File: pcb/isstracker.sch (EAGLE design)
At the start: 26 parts, among them IC2 L7805CV, J1 MOTOR_RIGHT, J2 MOTOR, J3 MOTOR_LEFT, J4 DISPLAY, J5 GLOBE_RESET, J6 CONTROL, J8 UART, J9 DISTANCE, Q2 60V/32A/35mΩ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

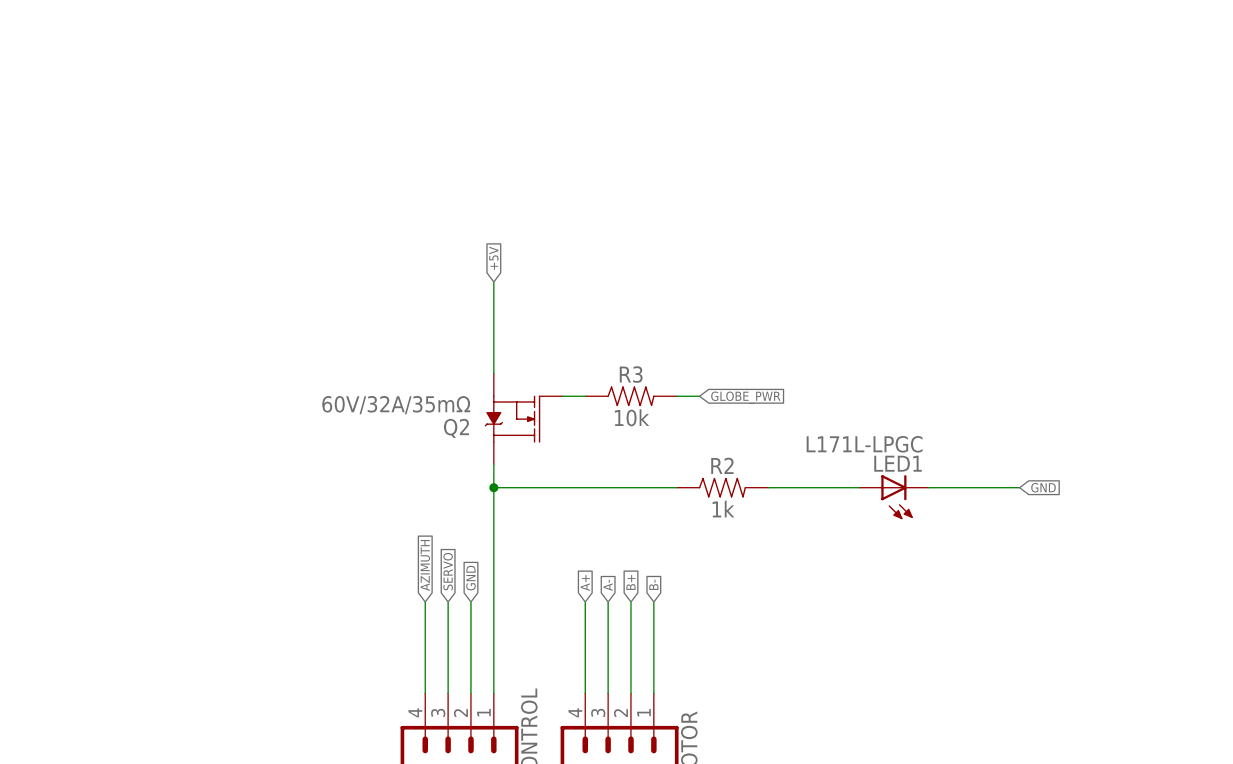
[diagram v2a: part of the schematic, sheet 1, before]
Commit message: Update to version 1.9
* Fix the FET, it wasn't right
* New FET in the BOM
* Put FET on low side and add pulldown on gate
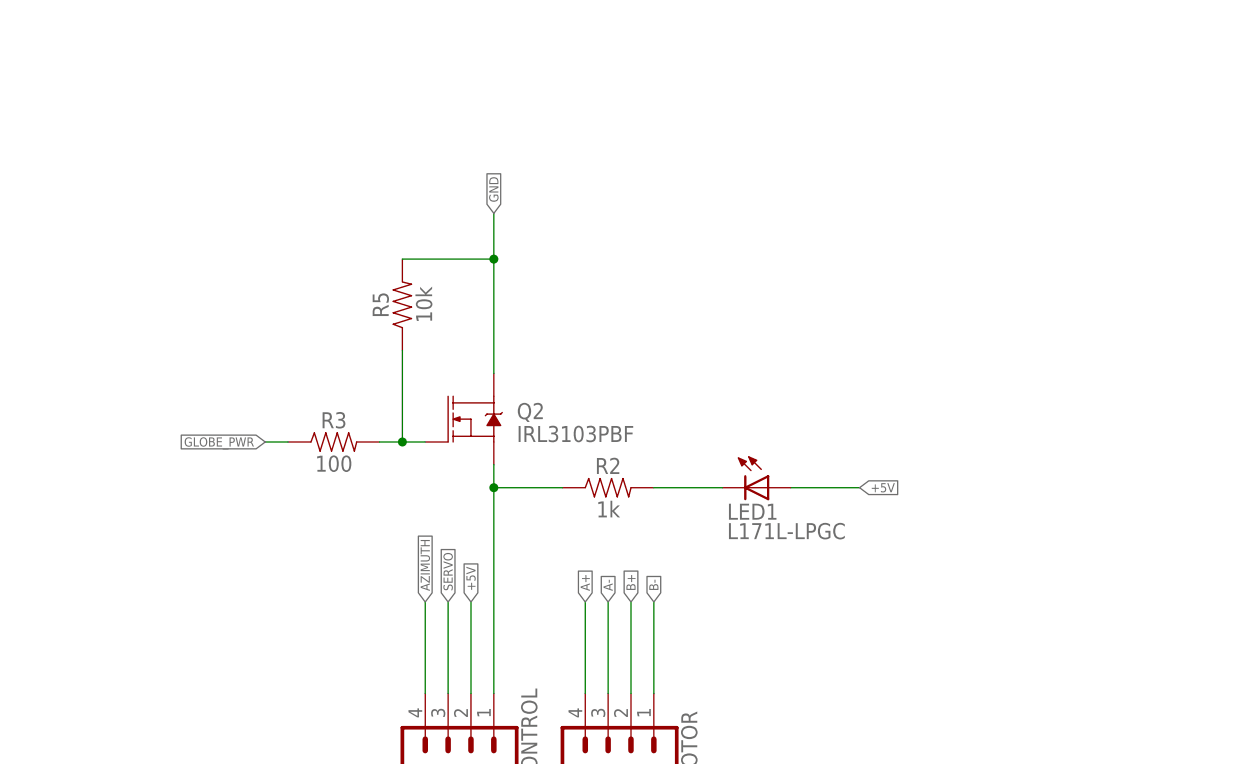
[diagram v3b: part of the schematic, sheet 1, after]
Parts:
- added R5: 10k, SparkFun-Resistors:0.75OHM-0805-1/4W-1%
- Q2: value 60V/32A/35mΩ -> IRL3103PBF
- R3: value 10k -> 100
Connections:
- removed net N$3: J6.1, Q2.D, R2.1
- removed net N$6: Q2.G, R3.1
- new net N$5: Q2.G, R3.2, R5.1
- new net N$8: J6.1, Q2.S, R2.1
- net +5V: now also J6.2, LED1.A; no longer Q2.S
- net GLOBE_PWR: now also R3.1; no longer R3.2
- net GND: now also Q2.D, R5.2; no longer J6.2, LED1.C
- net N$4: now also LED1.C; no longer LED1.A
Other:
- moved on the sheet: LED1, Q2, R2, R3
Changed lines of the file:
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@@
 <part name="J2" library="SparkFun-Connectors" library_urn="urn:adsk.eagle:library:513" deviceset="CONN_04" device="" package3d_urn="urn:adsk.eagle:package:38085/1" value="MOTOR"/>
 <part name="J6" library="SparkFun-Connectors" library_urn="urn:adsk.eagle:library:513" deviceset="CONN_04" device="" package3d_urn="urn:adsk.eagle:package:38085/1" value="CONTROL"/>
-<part name="Q2" library="SparkFun-DiscreteSemi" library_urn="urn:adsk.eagle:library:514" deviceset="MOSFET-NCH" device="-FQP30N06L" package3d_urn="urn:adsk.eagle:package:38447/1" value="60V/32A/35mΩ"/>
+<part name="Q2" library="SparkFun-DiscreteSemi" library_urn="urn:adsk.eagle:library:514" deviceset="MOSFET-NCH" device="-FQP30N06L" package3d_urn="urn:adsk.eagle:package:38447/1" value="IRL3103PBF "/>
 <part name="R2" library="SparkFun-Resistors" library_urn="urn:adsk.eagle:library:532" deviceset="0.75OHM" device="-0805-1/4W-1%" package3d_urn="urn:adsk.eagle:package:39651/1" value="1k"/>
 <part name="H6" library="holes" library_urn="urn:adsk.eagle:library:237" deviceset="MOUNT-HOLE" device="2.8" package3d_urn="urn:adsk.eagle:package:14271/1"/>
-<part name="R3" library="SparkFun-Resistors" library_urn="urn:adsk.eagle:library:532" deviceset="0.75OHM" device="-0805-1/4W-1%" package3d_urn="urn:adsk.eagle:package:39651/1" value="10k"/>
 <part name="LED3" library="adafruit" library_urn="urn:adsk.eagle:library:420" deviceset="LED" device="CHIPLED_1206" package3d_urn="urn:adsk.eagle:package:6240560/1" value="L171L-LPGC"/>
 <part name="LED1" library="adafruit" library_urn="urn:adsk.eagle:library:420" deviceset="LED" device="CHIPLED_1206" package3d_urn="urn:adsk.eagle:package:6240560/1" value="L171L-LPGC"/>
 <part name="J5" library="SparkFun-Connectors" library_urn="urn:adsk.eagle:library:513" deviceset="CONN_02" device="" package3d_urn="urn:adsk.eagle:package:38039/1" value="GLOBE_RESET"/>
 <part name="R4" library="SparkFun-Resistors" library_urn="urn:adsk.eagle:library:532" deviceset="0.75OHM" device="-0805-1/4W-1%" package3d_urn="urn:adsk.eagle:package:39651/1" value="10k"/>
+<part name="R5" library="SparkFun-Resistors" library_urn="urn:adsk.eagle:library:532" deviceset="0.75OHM" device="-0805-1/4W-1%" package3d_urn="urn:adsk.eagle:package:39651/1" value="10k"/>
+<part name="R3" library="SparkFun-Resistors" library_urn="urn:adsk.eagle:library:532" deviceset="0.75OHM" device="-0805-1/4W-1%" package3d_urn="urn:adsk.eagle:package:39651/1" value="100"/>
 </parts>
 <sheets>
@@
 <attribute name="NAME" x="101.092" y="33.02" size="1.778" layer="95" font="vector" rot="R90"/>
 </instance>
-<instance part="Q2" gate="NMOS" x="114.3" y="73.66" smashed="yes" rot="R180">
-<attribute name="NAME" x="109.22" y="73.66" size="1.778" layer="95" font="vector" rot="R180"/>
-<attribute name="VALUE" x="109.22" y="76.2" size="1.778" layer="96" font="vector" rot="R180"/>
-</instance>
-<instance part="R2" gate="G$1" x="137.16" y="66.04" smashed="yes">
-<attribute name="NAME" x="137.16" y="67.564" size="1.778" layer="95" font="vector" align="bottom-center"/>
-<attribute name="VALUE" x="137.16" y="64.516" size="1.778" layer="96" font="vector" align="top-center"/>
-</instance>
-<instance part="R3" gate="G$1" x="127" y="76.2" smashed="yes">
-<attribute name="NAME" x="127" y="77.724" size="1.778" layer="95" font="vector" align="bottom-center"/>
-<attribute name="VALUE" x="127" y="74.676" size="1.778" layer="96" font="vector" align="top-center"/>
-</instance>
-<instance part="LED1" gate="G$1" x="154.94" y="66.04" smashed="yes" rot="R90">
-<attribute name="NAME" x="159.512" y="69.596" size="1.778" layer="95" rot="R180"/>
-<attribute name="VALUE" x="159.512" y="71.755" size="1.778" layer="96" rot="R180"/>
+<instance part="Q2" gate="NMOS" x="109.22" y="73.66" smashed="yes">
+<attribute name="NAME" x="114.3" y="73.66" size="1.778" layer="95" font="vector"/>
+<attribute name="VALUE" x="114.3" y="71.12" size="1.778" layer="96" font="vector"/>
+</instance>
+<instance part="R2" gate="G$1" x="124.46" y="66.04" smashed="yes">
+<attribute name="NAME" x="124.46" y="67.564" size="1.778" layer="95" font="vector" align="bottom-center"/>
+<attribute name="VALUE" x="124.46" y="64.516" size="1.778" layer="96" font="vector" align="top-center"/>
+</instance>
+<instance part="LED1" gate="G$1" x="142.24" y="66.04" smashed="yes" rot="R270">
+<attribute name="NAME" x="137.668" y="62.484" size="1.778" layer="95"/>
+<attribute name="VALUE" x="137.668" y="60.325" size="1.778" layer="96"/>
 </instance>
 <instance part="J5" gate="G$1" x="12.7" y="116.84" smashed="yes">
@@
 <attribute name="NAME" x="28.956" y="111.76" size="1.778" layer="95" font="vector" rot="R90" align="bottom-center"/>
 <attribute name="VALUE" x="32.004" y="111.76" size="1.778" layer="96" font="vector" rot="R90" align="top-center"/>
+</instance>
+<instance part="R5" gate="G$1" x="101.6" y="86.36" smashed="yes" rot="R90">
+<attribute name="NAME" x="100.076" y="86.36" size="1.778" layer="95" font="vector" rot="R90" align="bottom-center"/>
+<attribute name="VALUE" x="103.124" y="86.36" size="1.778" layer="96" font="vector" rot="R90" align="top-center"/>
+</instance>
+<instance part="R3" gate="G$1" x="93.98" y="71.12" smashed="yes">
+<attribute name="NAME" x="93.98" y="72.644" size="1.778" layer="95" font="vector" align="bottom-center"/>
+<attribute name="VALUE" x="93.98" y="69.596" size="1.778" layer="96" font="vector" align="top-center"/>
 </instance>
 </instances>
@@
 </segment>
 <segment>
-<wire x1="109.22" y1="43.18" x2="109.22" y2="53.34" width="0.1524" layer="91"/>
-<label x="109.22" y="53.34" size="1.016" layer="95" rot="R90" xref="yes"/>
-<pinref part="J6" gate="G$1" pin="2"/>
-</segment>
-<segment>
-<wire x1="160.02" y1="66.04" x2="170.18" y2="66.04" width="0.1524" layer="91"/>
-<label x="170.18" y="66.04" size="1.016" layer="95" xref="yes"/>
-<pinref part="LED1" gate="G$1" pin="C"/>
-</segment>
-<segment>
 <pinref part="J3" gate="G$1" pin="12"/>
 <wire x1="20.32" y1="160.02" x2="27.94" y2="160.02" width="0.1524" layer="91"/>
@@
 <label x="43.18" y="119.38" size="1.016" layer="95" xref="yes"/>
 </segment>
+<segment>
+<pinref part="Q2" gate="NMOS" pin="D"/>
+<pinref part="R5" gate="G$1" pin="2"/>
+<wire x1="111.76" y1="78.74" x2="111.76" y2="91.44" width="0.1524" layer="91"/>
+<wire x1="111.76" y1="91.44" x2="111.76" y2="96.52" width="0.1524" layer="91"/>
+<wire x1="101.6" y1="91.44" x2="111.76" y2="91.44" width="0.1524" layer="91"/>
+<junction x="111.76" y="91.44"/>
+<label x="111.76" y="96.52" size="1.016" layer="95" rot="R90" xref="yes"/>
+</segment>
 </net>
 <net name="+5V" class="0">
@@
 </segment>
 <segment>
-<wire x1="111.76" y1="78.74" x2="111.76" y2="88.9" width="0.1524" layer="91"/>
-<label x="111.76" y="88.9" size="1.016" layer="95" rot="R90" xref="yes"/>
-<pinref part="Q2" gate="NMOS" pin="S"/>
+<pinref part="J6" gate="G$1" pin="2"/>
+<wire x1="109.22" y1="43.18" x2="109.22" y2="53.34" width="0.1524" layer="91"/>
+<label x="109.22" y="53.34" size="1.016" layer="95" rot="R90" xref="yes"/>
+</segment>
+<segment>
+<pinref part="LED1" gate="G$1" pin="A"/>
+<wire x1="144.78" y1="66.04" x2="152.4" y2="66.04" width="0.1524" layer="91"/>
+<label x="152.4" y="66.04" size="1.016" layer="95" xref="yes"/>
 </segment>
 </net>
@@
 </segment>
 </net>
-<net name="N$3" class="0">
-<segment>
-<pinref part="J6" gate="G$1" pin="1"/>
-<wire x1="111.76" y1="43.18" x2="111.76" y2="66.04" width="0.1524" layer="91"/>
-<pinref part="Q2" gate="NMOS" pin="D"/>
-<pinref part="R2" gate="G$1" pin="1"/>
-<wire x1="111.76" y1="66.04" x2="111.76" y2="68.58" width="0.1524" layer="91"/>
-<wire x1="132.08" y1="66.04" x2="111.76" y2="66.04" width="0.1524" layer="91"/>
-<junction x="111.76" y="66.04"/>
-</segment>
-</net>
-<net name="N$4" class="0">
-<segment>
-<pinref part="R2" gate="G$1" pin="2"/>
-<wire x1="142.24" y1="66.04" x2="152.4" y2="66.04" width="0.1524" layer="91"/>
-<pinref part="LED1" gate="G$1" pin="A"/>
-</segment>
-</net>
-<net name="N$6" class="0">
-<segment>
-<pinref part="Q2" gate="NMOS" pin="G"/>
-<pinref part="R3" gate="G$1" pin="1"/>
-<wire x1="119.38" y1="76.2" x2="121.92" y2="76.2" width="0.1524" layer="91"/>
-</segment>
-</net>
 <net name="GLOBE_PWR" class="0">
 <segment>
@@
 </segment>
 <segment>
-<pinref part="R3" gate="G$1" pin="2"/>
-<wire x1="134.62" y1="76.2" x2="132.08" y2="76.2" width="0.1524" layer="91"/>
-<label x="134.62" y="76.2" size="1.016" layer="95" xref="yes"/>
+<pinref part="R3" gate="G$1" pin="1"/>
+<wire x1="88.9" y1="71.12" x2="86.36" y2="71.12" width="0.1524" layer="91"/>
+<label x="86.36" y="71.12" size="1.016" layer="95" rot="R180" xref="yes"/>
 </segment>
 </net>
@@
 </segment>
 </net>
+<net name="N$5" class="0">
+<segment>
+<pinref part="Q2" gate="NMOS" pin="G"/>
+<pinref part="R3" gate="G$1" pin="2"/>
+<wire x1="104.14" y1="71.12" x2="101.6" y2="71.12" width="0.1524" layer="91"/>
+<pinref part="R5" gate="G$1" pin="1"/>
+<wire x1="101.6" y1="71.12" x2="99.06" y2="71.12" width="0.1524" layer="91"/>
+<wire x1="101.6" y1="81.28" x2="101.6" y2="71.12" width="0.1524" layer="91"/>
+<junction x="101.6" y="71.12"/>
+</segment>
+</net>
+<net name="N$8" class="0">
+<segment>
+<pinref part="J6" gate="G$1" pin="1"/>
+<pinref part="Q2" gate="NMOS" pin="S"/>
+<wire x1="111.76" y1="43.18" x2="111.76" y2="66.04" width="0.1524" layer="91"/>
+<pinref part="R2" gate="G$1" pin="1"/>
+<wire x1="111.76" y1="66.04" x2="111.76" y2="68.58" width="0.1524" layer="91"/>
+<wire x1="119.38" y1="66.04" x2="111.76" y2="66.04" width="0.1524" layer="91"/>
+<junction x="111.76" y="66.04"/>
+</segment>
+</net>
+<net name="N$4" class="0">
+<segment>
+<pinref part="R2" gate="G$1" pin="2"/>
+<pinref part="LED1" gate="G$1" pin="C"/>
+<wire x1="129.54" y1="66.04" x2="137.16" y2="66.04" width="0.1524" layer="91"/>
+</segment>
+</net>

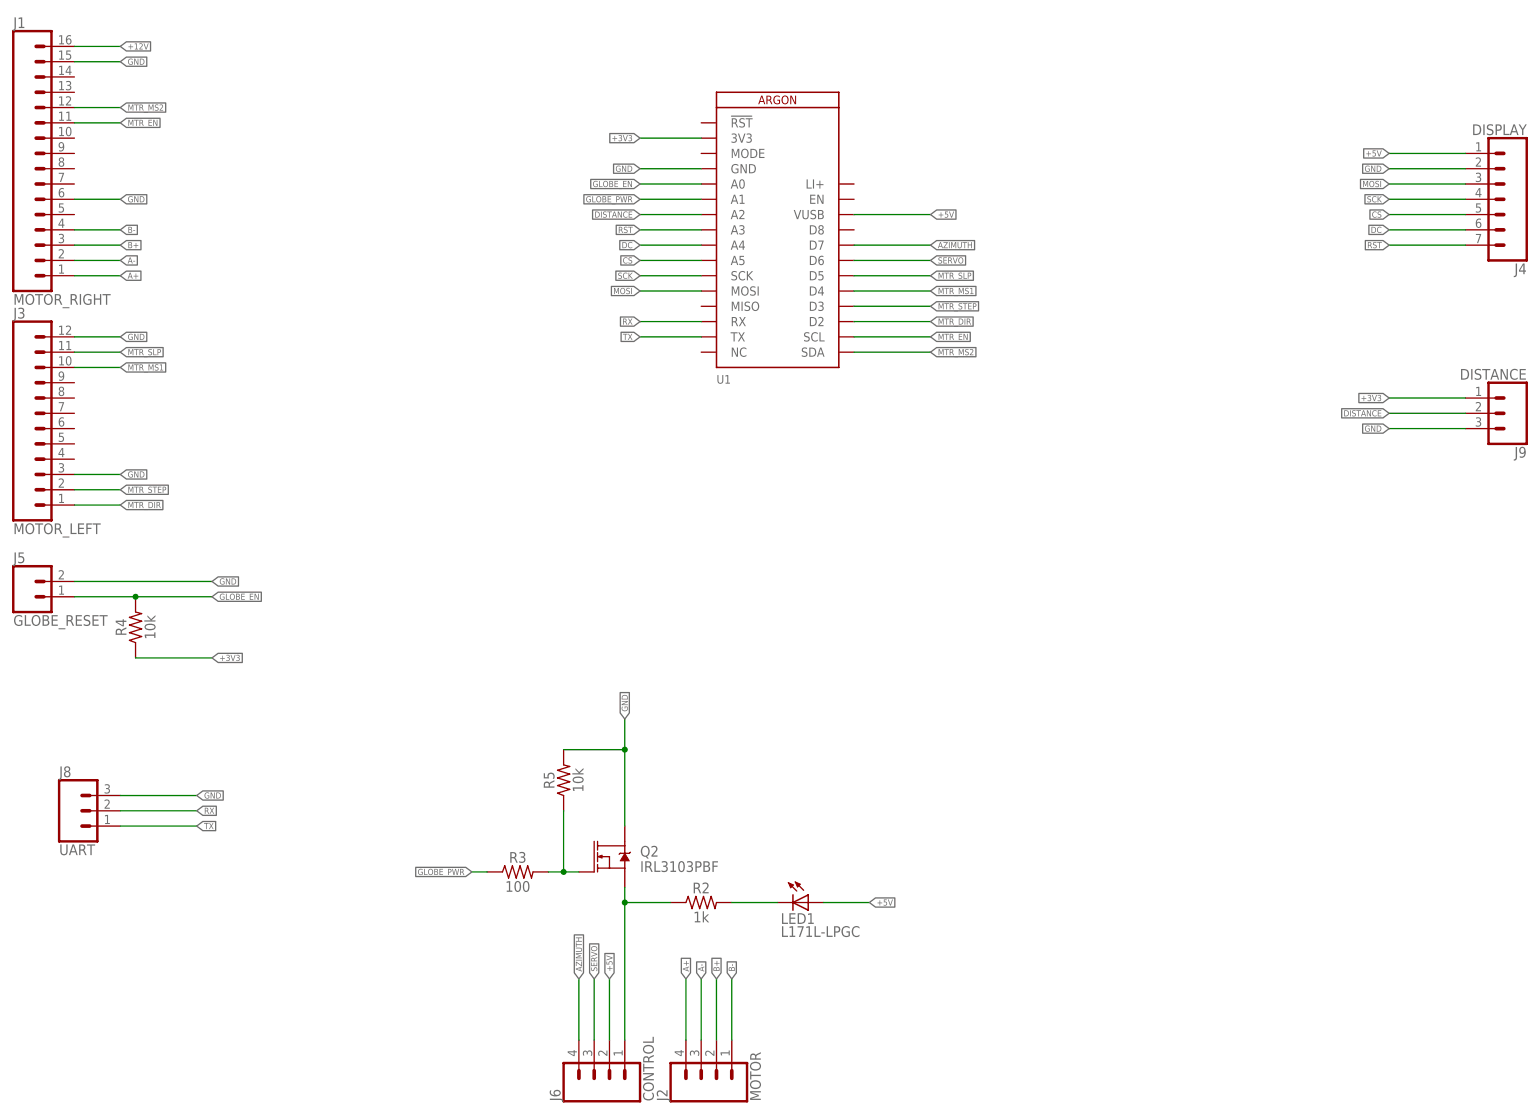
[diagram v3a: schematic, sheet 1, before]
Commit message: Fixes
* Add globe power using a MOSFET so the laser can be turned on/off
* Update both board layouts to accomodate new power scheme
* Fix some component positions in layout
* Migrate to screw terminals for power on board
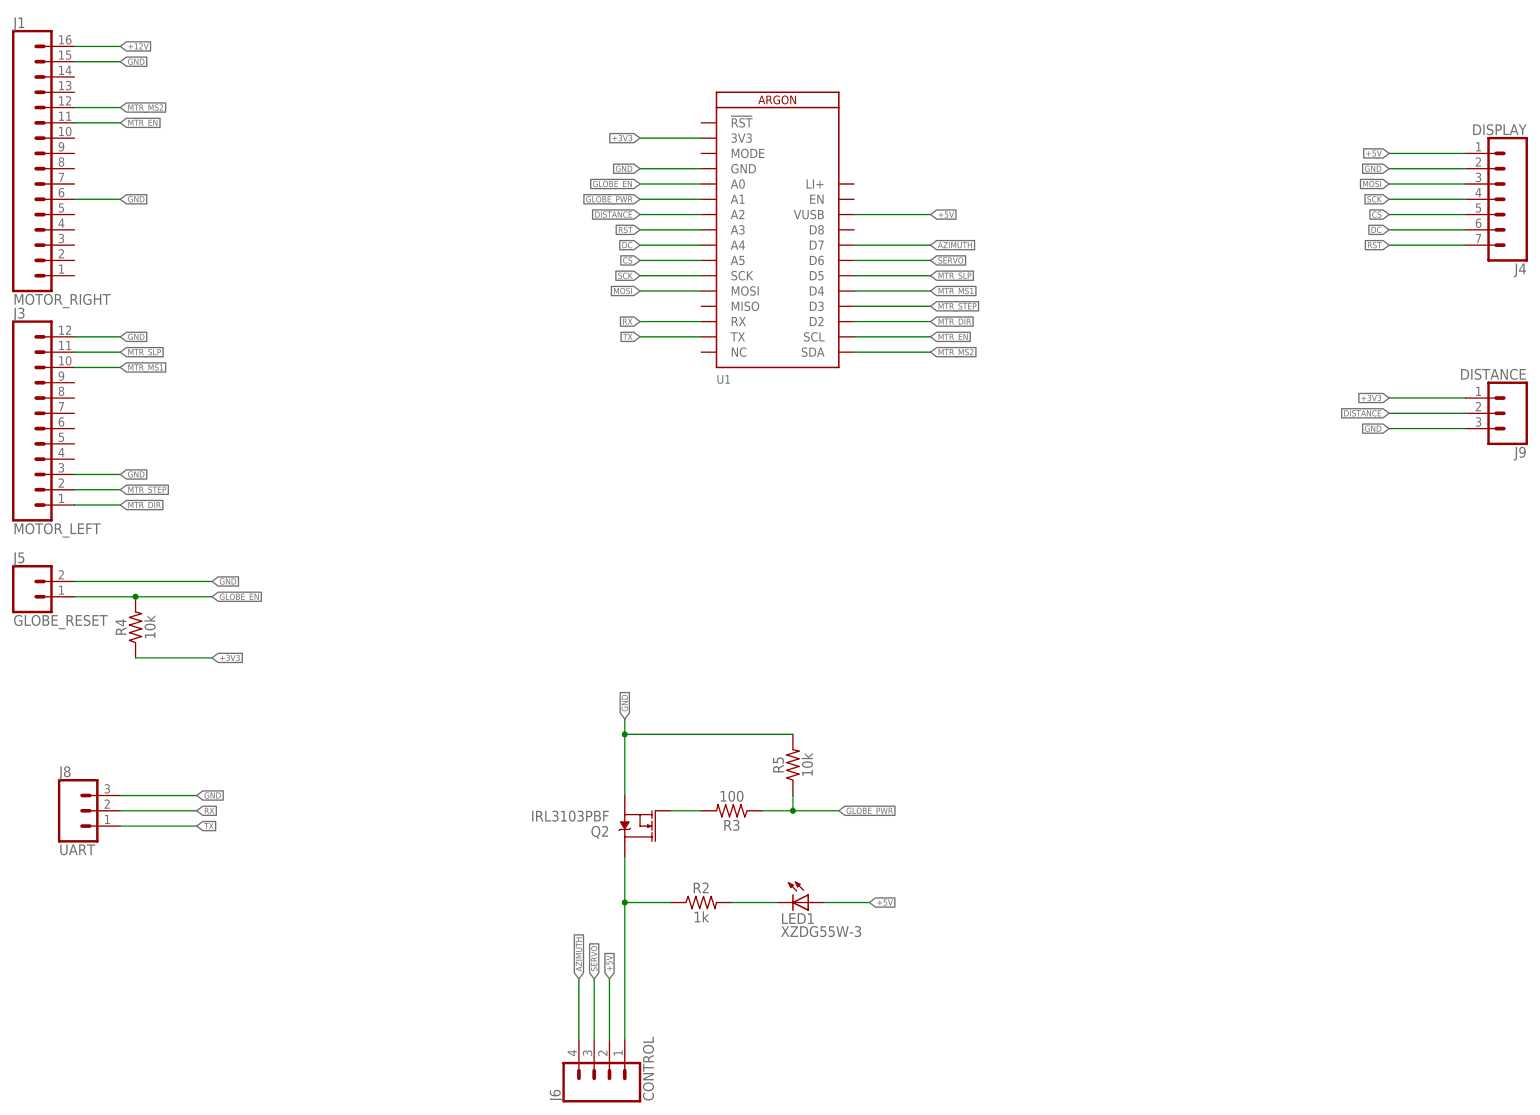
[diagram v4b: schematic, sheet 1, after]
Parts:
- removed LED3: L171L-LPGC, adafruit:LEDCHIPLED_1206
- removed X1: +12V, con-molex:KK-156-2
- added H5: MOUNT-HOLE2.8, holes:MOUNT-HOLE2.8
- added LED2: XZDG55W-3, adafruit:LEDCHIPLED_1206
- J2: value MOTOR -> (none); device SparkFun-Connectors:CONN_04 -> SparkFun-Connectors:CONN_03LOCK_LONGPADS
- LED1: value L171L-LPGC -> XZDG55W-3
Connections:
- removed net A+: J1.1, J2.4
- removed net A-: J1.2, J2.3
- removed net B+: J1.3, J2.2
- removed net B-: J1.4, J2.1
- removed net N$5: Q2.G, R3.2, R5.1
- new net N$3: Q2.G, R3.2
- net +12V: now also LED2.A; no longer R1.2
- net GLOBE_PWR: now also R5.1
- net GND: now also J2.1, Q2.S, R1.1; no longer LED3.C, Q2.D, X1-2.S
- net N$1: now also J2.3; no longer X1-1.S
- net N$2: now also LED2.C, R1.2; no longer LED3.A, R1.1
- net N$8: now also Q2.D; no longer Q2.S
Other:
- moved on the sheet: Q2, R1, R3, R5
